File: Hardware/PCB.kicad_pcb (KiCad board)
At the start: 2 copper layers, 43 parts, among them J1 Conn_01x15, J2 Conn_01x15, J3 Conn_01x19, J4 Conn_01x19, Q5 NMOS, Q6 NMOS, Q7 NMOS, Q8 NMOS, U10 TLV379IDR, U11 LM780_TO220_MA BYC_3V_BO_POJD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

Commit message: 1
1
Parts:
- moved R13 12.1 mm to (82.0, 120.5), turned to -90 degrees
- moved R18 12.1 mm to (102.0, 120.5), turned to -90 degrees
- moved R16 7.13 mm to (99.8, 115.3), turned to -90 degrees
- moved R14 6.16 mm to (79.4, 115.1), turned to -90 degrees
- moved U8 3.33 mm to (105.5, 113.7)
- moved U9 3.26 mm to (85.5, 113.7)
- moved C17 3.23 mm to (71.5, 114.5), turned to 90 degrees
- moved C18 2.98 mm to (91.5, 114.5), turned to 90 degrees
- moved C23 2.34 mm to (85.0, 120.5)
- moved C13 2.25 mm to (105.0, 120.5)
- moved D4 2.24 mm to (106.2, 125.0)
- moved D6 2.24 mm to (86.2, 125.0)
- moved R12 1.93 mm to (88.0, 120.5)
- moved R10 1.67 mm to (108.0, 120.5)
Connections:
- Q7 pad 2: Net-(Q5-D) -> Net-(Q7-G)
- Q8 pad 2: Net-(Q5-D) -> Net-(Q8-G)
- R16 pad 2: Net-(Q5-D) -> Net-(Q8-G)
- R18 pad 2: Net-(Q5-D) -> Net-(Q7-G)
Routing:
- net Net-(Q5-G): track 18.0 -> 0.00 mm, vias 1 -> 0
- net Net-(Q7-S): track 0.00 -> 17.0 mm, vias 0 -> 2
- net Net-(D6-K): track 14.6 -> 0.00 mm
- net Net-(Q8-G): track 0.00 -> 8.89 mm, vias 0 -> 2
- net Net-(U9-HO): track 8.67 -> 0.00 mm, vias 2 -> 0
- net Net-(U10-V+): track 5.06 -> 0.00 mm
- net Net-(U9-LO): track 5.06 -> 0.00 mm, vias 2 -> 0
- net Net-(U8-LO): track 0.00 -> 4.73 mm
- net Net-(Q6-G): track 4.76 -> 0.25 mm
- net Net-(Q5-S): track 13.7 -> 11.5 mm
- net Net-(D6-A): track 3.42 -> 1.42 mm
- net (no net): vias 0 -> 2

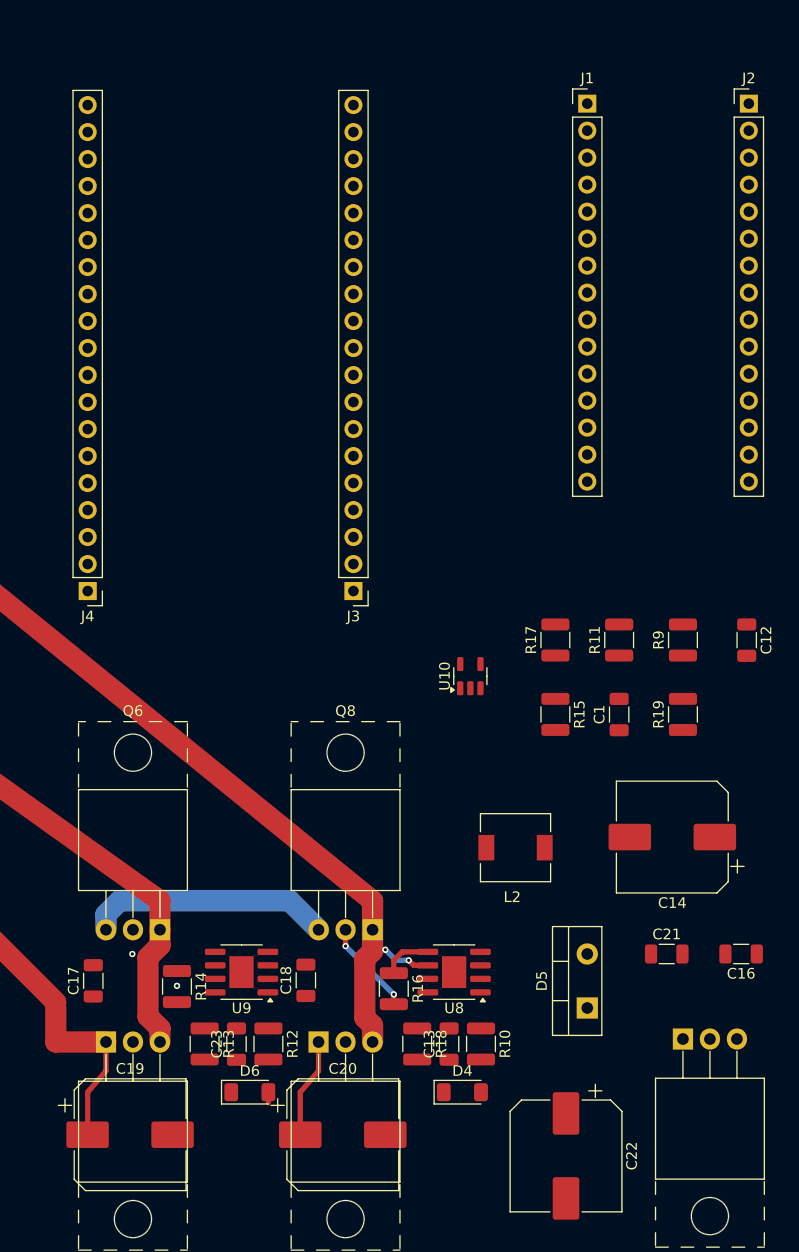
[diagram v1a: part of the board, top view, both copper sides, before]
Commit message: 1
Część finalna połączona, trzeba zrobić pole GND i zrobić przelotki GND
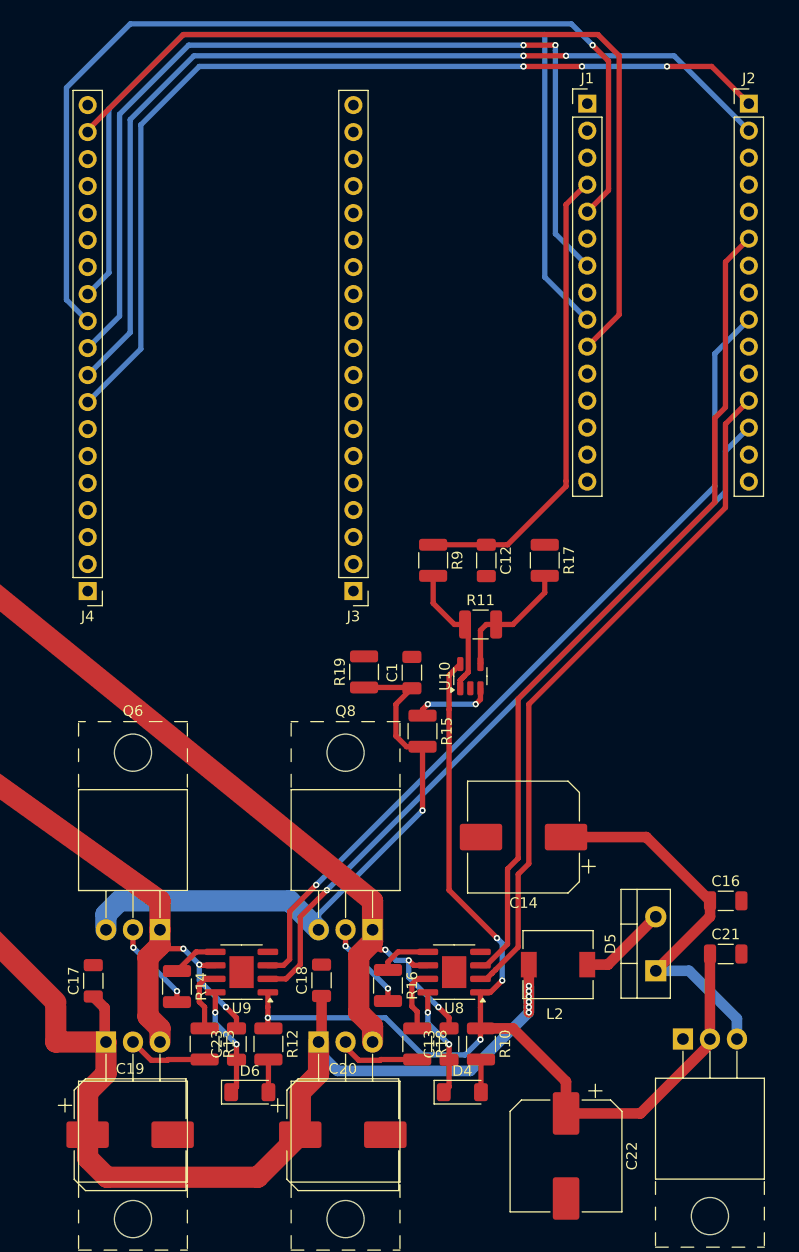
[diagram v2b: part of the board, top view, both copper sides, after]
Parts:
- moved R19 30.3 mm to (97.0, 85.5)
- moved C12 25.6 mm to (108.5, 75.0)
- moved R9 24.7 mm to (103.5, 75.0), turned to -90 degrees
- moved C1 19.9 mm to (101.5, 85.5)
- moved C14 14.0 mm to (112.0, 101.0)
- moved R11 13.1 mm to (108.0, 81.0), turned to 0 degrees
- moved R15 12.6 mm to (102.5, 91.0)
- moved L2 11.7 mm to (115.2, 113.0)
- moved R17 7.57 mm to (114.0, 75.0), turned to -90 degrees
- moved D5 7.33 mm to (124.4, 113.6)
- moved C21 5.55 mm to (131.0, 112.0)
- moved C16 5.21 mm to (131.0, 107.0), turned to 0 degrees
- moved C18 1.47 mm to (93.0, 114.5)
- moved R16 0.63 mm to (99.2, 115.0)
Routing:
- net Net-(U10-V+): track 0.00 -> 102.5 mm, vias 0 -> 4
- net /SCK: track 0.00 -> 92.7 mm, vias 0 -> 1
- net /MISO: track 0.00 -> 90.6 mm
- net /RX: track 0.00 -> 89.3 mm, vias 0 -> 2
- net /TX: track 0.00 -> 89.1 mm, vias 0 -> 3
- net /CC: track 0.00 -> 88.9 mm, vias 0 -> 2
- net Net-(Q5-D): track 30.7 -> 114.3 mm, vias 0 -> 6
- net /MOSI: track 0.00 -> 83.3 mm
- net Net-(J2-Pin_9): track 0.00 -> 80.4 mm, vias 0 -> 1
- net Net-(J2-Pin_6): track 0.00 -> 79.2 mm
- net Net-(J2-Pin_13): track 0.00 -> 71.6 mm, vias 0 -> 1
- net Net-(J2-Pin_12): track 0.00 -> 65.2 mm
- net Net-(J1-Pin_4): track 0.00 -> 44.1 mm
- net Net-(D5-K): track 0.00 -> 36.1 mm
- net Net-(Q6-S): track 23.1 -> 56.9 mm, vias 0 -> 1
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
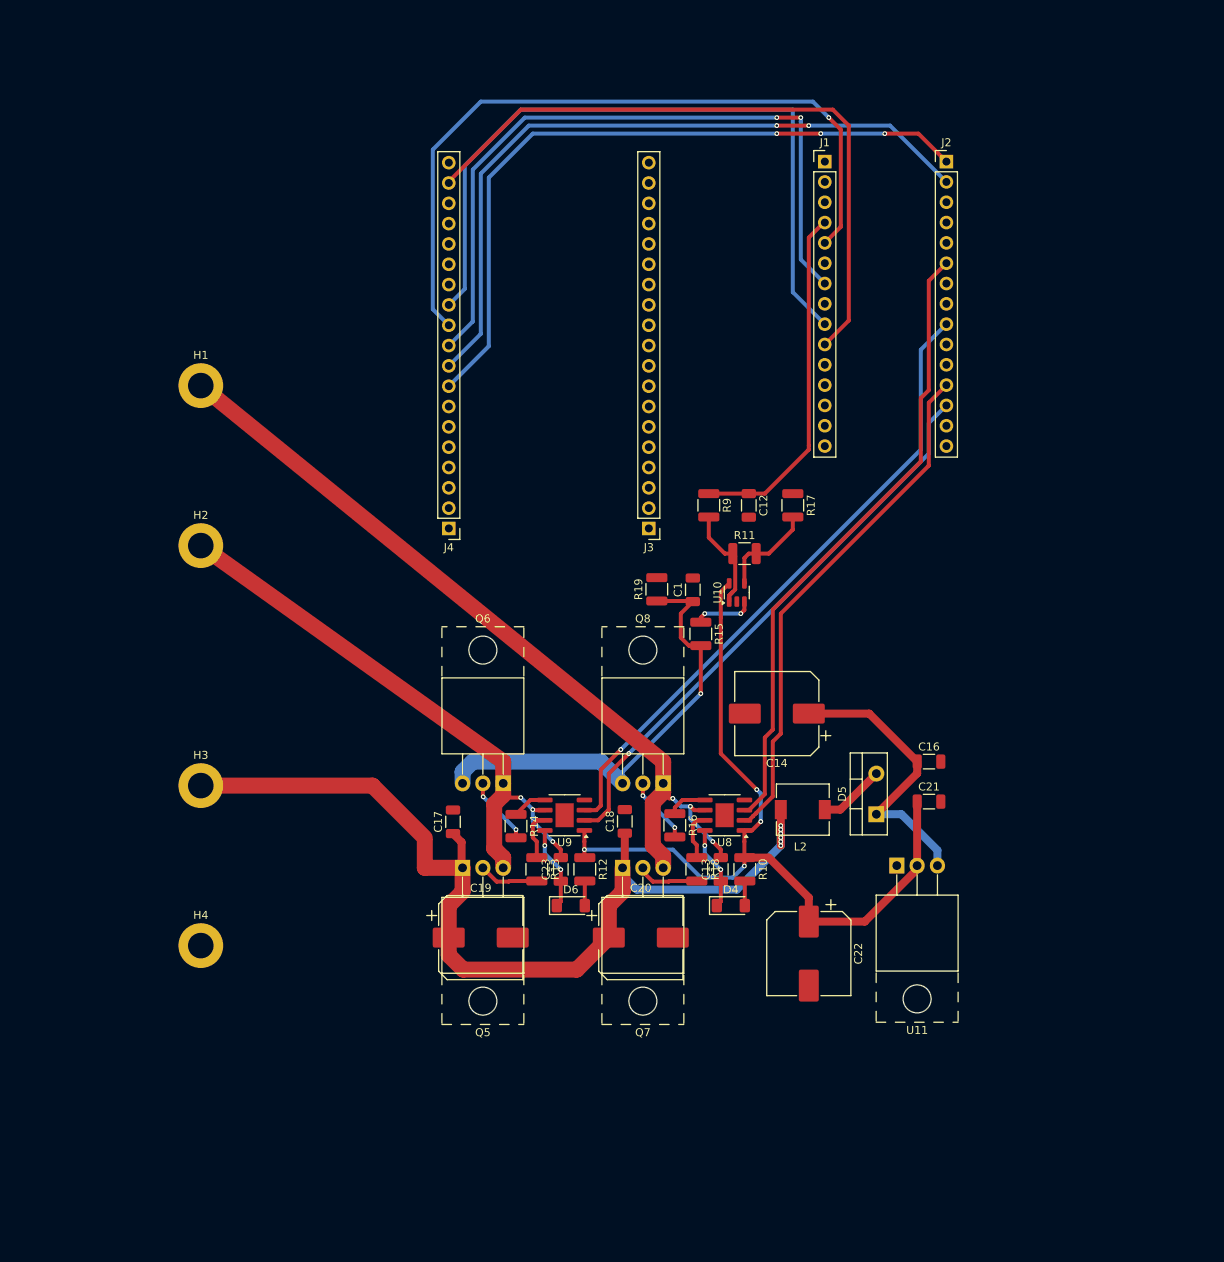
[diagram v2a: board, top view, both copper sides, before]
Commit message: 1
trzeba zrobić pole gnd, przelotki gnd i ustawić wymiary pcb
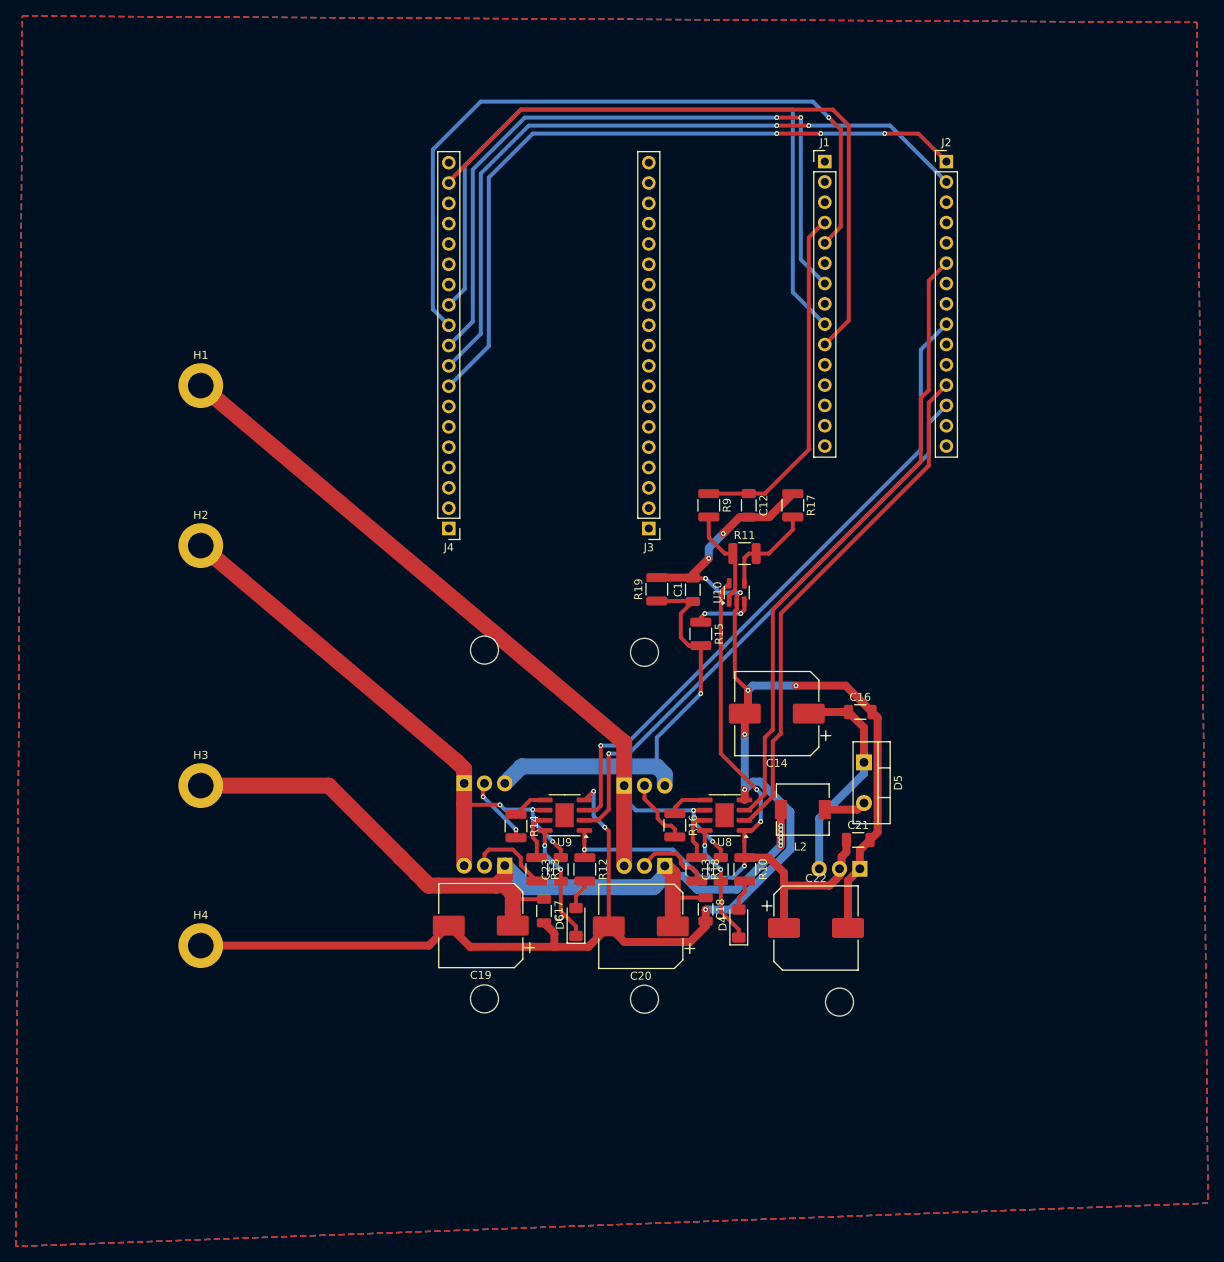
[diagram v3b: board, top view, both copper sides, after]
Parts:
- Q5, Q6, Q7, Q8: moved to B.Cu
- U11: value LM780_TO220_MA BYC_3V_BO_POJDZIE_Z_DYMEM -> LM7803; moved to B.Cu
- moved C17 15.9 mm to (82.9, 125.7), turned to -90 degrees
- moved C18 14.9 mm to (103.1, 125.5), turned to -90 degrees
- moved C16 10.6 mm to (122.4, 100.8)
- moved C21 10.1 mm to (122.2, 116.8)
- moved D5 6.66 mm to (122.9, 107.1), turned to -90 degrees
- moved Q5 5.29 mm to (78.0, 120.0), turned to 180 degrees
- moved Q7 5.29 mm to (98.0, 120.0), turned to 180 degrees
- moved Q8 4.89 mm to (92.9, 110.0), turned to 0 degrees
- moved Q6 4.88 mm to (72.9, 109.7), turned to 0 degrees
- moved U11 4.64 mm to (122.4, 120.4), turned to 180 degrees
- moved C22 3.32 mm to (116.9, 127.8), turned to 0 degrees
- moved D4 2.46 mm to (107.2, 127.2), turned to 90 degrees
- moved D6 2.15 mm to (86.9, 127.0), turned to 90 degrees
- moved C19 1.50 mm to (75.0, 127.5), turned to 180 degrees
- moved C20 1.40 mm to (95.0, 127.6), turned to 180 degrees
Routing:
- net GND: track 0.00 -> 221.1 mm, vias 0 -> 11
- net Net-(U10-V+): track 102.5 -> 89.7 mm
- net Net-(D5-K): track 36.1 -> 27.8 mm
- net Net-(Q7-S): track 27.5 -> 35.6 mm, vias 3 -> 2
- net Net-(Q5-S): track 24.9 -> 31.4 mm
- net Net-(D4-K): track 10.4 -> 15.2 mm
- net Net-(D6-K): track 10.4 -> 14.8 mm
- net Net-(Q6-S): track 56.9 -> 52.6 mm
- net Net-(D5-A): track 8.31 -> 5.24 mm
- net Net-(Q7-G): track 7.76 -> 10.7 mm
- net Net-(Q5-G): track 7.48 -> 10.4 mm
- net Net-(J2-Pin_9): track 80.4 -> 82.1 mm
- net Net-(J2-Pin_13): track 71.6 -> 73.1 mm
- net Net-(Q5-D): track 114.3 -> 112.9 mm
- net Net-(D4-A): track 3.08 -> 3.89 mm
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- added copper zone on B.Cu, net GND
- added copper zone on F.Cu, net GND

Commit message: 1
trzeba zrobić siatkę przelotek i usunąć maskę z torów prądowych
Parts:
- moved C1 139.5 mm to (223.5, 153.2)
- moved C12 139.5 mm to (230.5, 142.7)
- moved C13 139.5 mm to (227.0, 188.2)
- moved C14 139.5 mm to (234.0, 168.7)
- moved C16 139.5 mm to (244.4, 168.5)
- moved C17 139.5 mm to (204.9, 193.4)
- moved C18 139.5 mm to (225.1, 193.2)
- moved C19 139.5 mm to (197.0, 195.2)
- moved C20 139.5 mm to (217.0, 195.3)
- moved C21 139.5 mm to (244.2, 184.5)
- moved C22 139.5 mm to (238.9, 195.5)
- moved C23 139.5 mm to (207.0, 188.2)
- moved D4 139.5 mm to (229.2, 194.9)
- moved D5 139.5 mm to (244.9, 174.8)
- moved D6 139.5 mm to (208.9, 194.7)
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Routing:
- net GND: track 221.1 -> 221.0 mm, vias 11 -> 24
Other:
- board outline added: 140 x 180 mm
- board text added: "STEROWNIK WIBRATORA WAGINALNEGO Autorzy projektu: Przemysław Lis Mateusz Kubsiewicz Jakub Banasiak Politechnka Wrocławska 2025"

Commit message: 1
1
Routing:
- net Net-(Q7-S): track 35.6 -> 110.1 mm
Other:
- board text added: "FALOWNIK Autorzy projektu: Przemysław Lis Mateusz Kubsiewicz Jakub Banasiak Politechnka Wrocławska 2025"
- board text removed: "STEROWNIK WIBRATORA WAGINALNEGO Autorzy projektu: Przemysław Lis Mateusz Kubsiewicz Jakub Banasiak Politechnka Wrocławska 2025"
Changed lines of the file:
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@@
-	)
-	(gr_line
-		(start 214.9 172.28)
-		(end 162 127.68)
-		(stroke
-			(width 2)
-			(type solid)
-		)
-		(layer "F.Cu")
-		(net 5)
 	)
 	(gr_line
@@
 		(layer "Edge.Cuts")
 	)
-	(gr_text "STEROWNIK WIBRATORA WAGINALNEGO\n\nAutorzy projektu:\nPrzemysław Lis\nMateusz Kubsiewicz\nJakub Banasiak\n\nPolitechnka Wrocławska 2025"
+	(gr_text "FALOWNIK\n\nAutorzy projektu:\nPrzemysław Lis\nMateusz Kubsiewicz\nJakub Banasiak\n\nPolitechnka Wrocławska 2025"
 		(at 215.6 242.2 0)
 		(layer "F.Cu")
@@
 	)
 	(segment
-		(start 214.9 172.28)
-		(end 214.92 172.3)
+		(start 214.92 177.68)
+		(end 214.92 176.52)
 		(width 2)
 		(layer "F.Cu")
@@
 	)
 	(segment
+		(start 187.2 153)
+		(end 162 127.8)
+		(width 2)
+		(layer "F.Cu")
+		(net 5)
+	)
+	(segment
+		(start 215 167.4)
+		(end 200.6 153)
+		(width 2)
+		(layer "F.Cu")
+		(net 5)
+	)
+	(segment
 		(start 223.6 180.78)
 		(end 224.97 180.78)
@@
 	)
 	(segment
+		(start 214.92 176.52)
+		(end 215 176.44)
+		(width 2)
+		(layer "F.Cu")
+		(net 5)
+	)
+	(segment
+		(start 215 176.44)
+		(end 215 167.4)
+		(width 2)
+		(layer "F.Cu")
+		(net 5)
+	)
+	(segment
 		(start 214.6 187.84)
 		(end 214.72 187.96)
@@
 	)
 	(segment
+		(start 200.6 153)
+		(end 187.2 153)
+		(width 2)
+		(layer "F.Cu")
+		(net 5)
+	)
+	(segment
 		(start 224.97 180.78)
 		(end 225 180.75)
@@
 	)
 	(segment
-		(start 214.92 172.3)
-		(end 214.92 177.68)
-		(width 2)
-		(layer "F.Cu")
+		(start 162 127.8)
+		(end 162 127.68)
+		(width 2)
+		(layer "F.Cu")
